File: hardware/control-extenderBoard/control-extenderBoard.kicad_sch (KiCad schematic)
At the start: 117 parts, among them J1 12V + GND (TP), J10 SCL6 + GND (TP), J11 SDA6 + GND (TP), J12 3V3 + GND (TP), J13 12V + GND (TP), J14 SCL6 + GND (TP), J15 SDA6 + GND (TP), J17 24V IN, J18 GND, J2 12V Out, J22 SDA, SCL - ESP32, J23 I2C Reserve SCL/GND, J24 I2C Reserve SCL/GND, J25 I2C Reserve SDA/GND, J26 I2C Reserve SDA/GND, J3 5V out, J4 3V3 + GND (TP), J5 GND, J6 SCL7 Differential (TP), J7 SDA7 Differential (TP), J8 RS485, J9 3V3 out, P1 ISP, U1 MAX3485, U10 LM2576T-12, U2 PCA9600D, U3 TCA9548A_1-to-8_I2C_Multiplex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, U4 LM2576T-3.3, U5 PCA9600D, U6 PCA82C251, U7 PCA82C251, U8 PCA9600D, U9 LM2576T-5

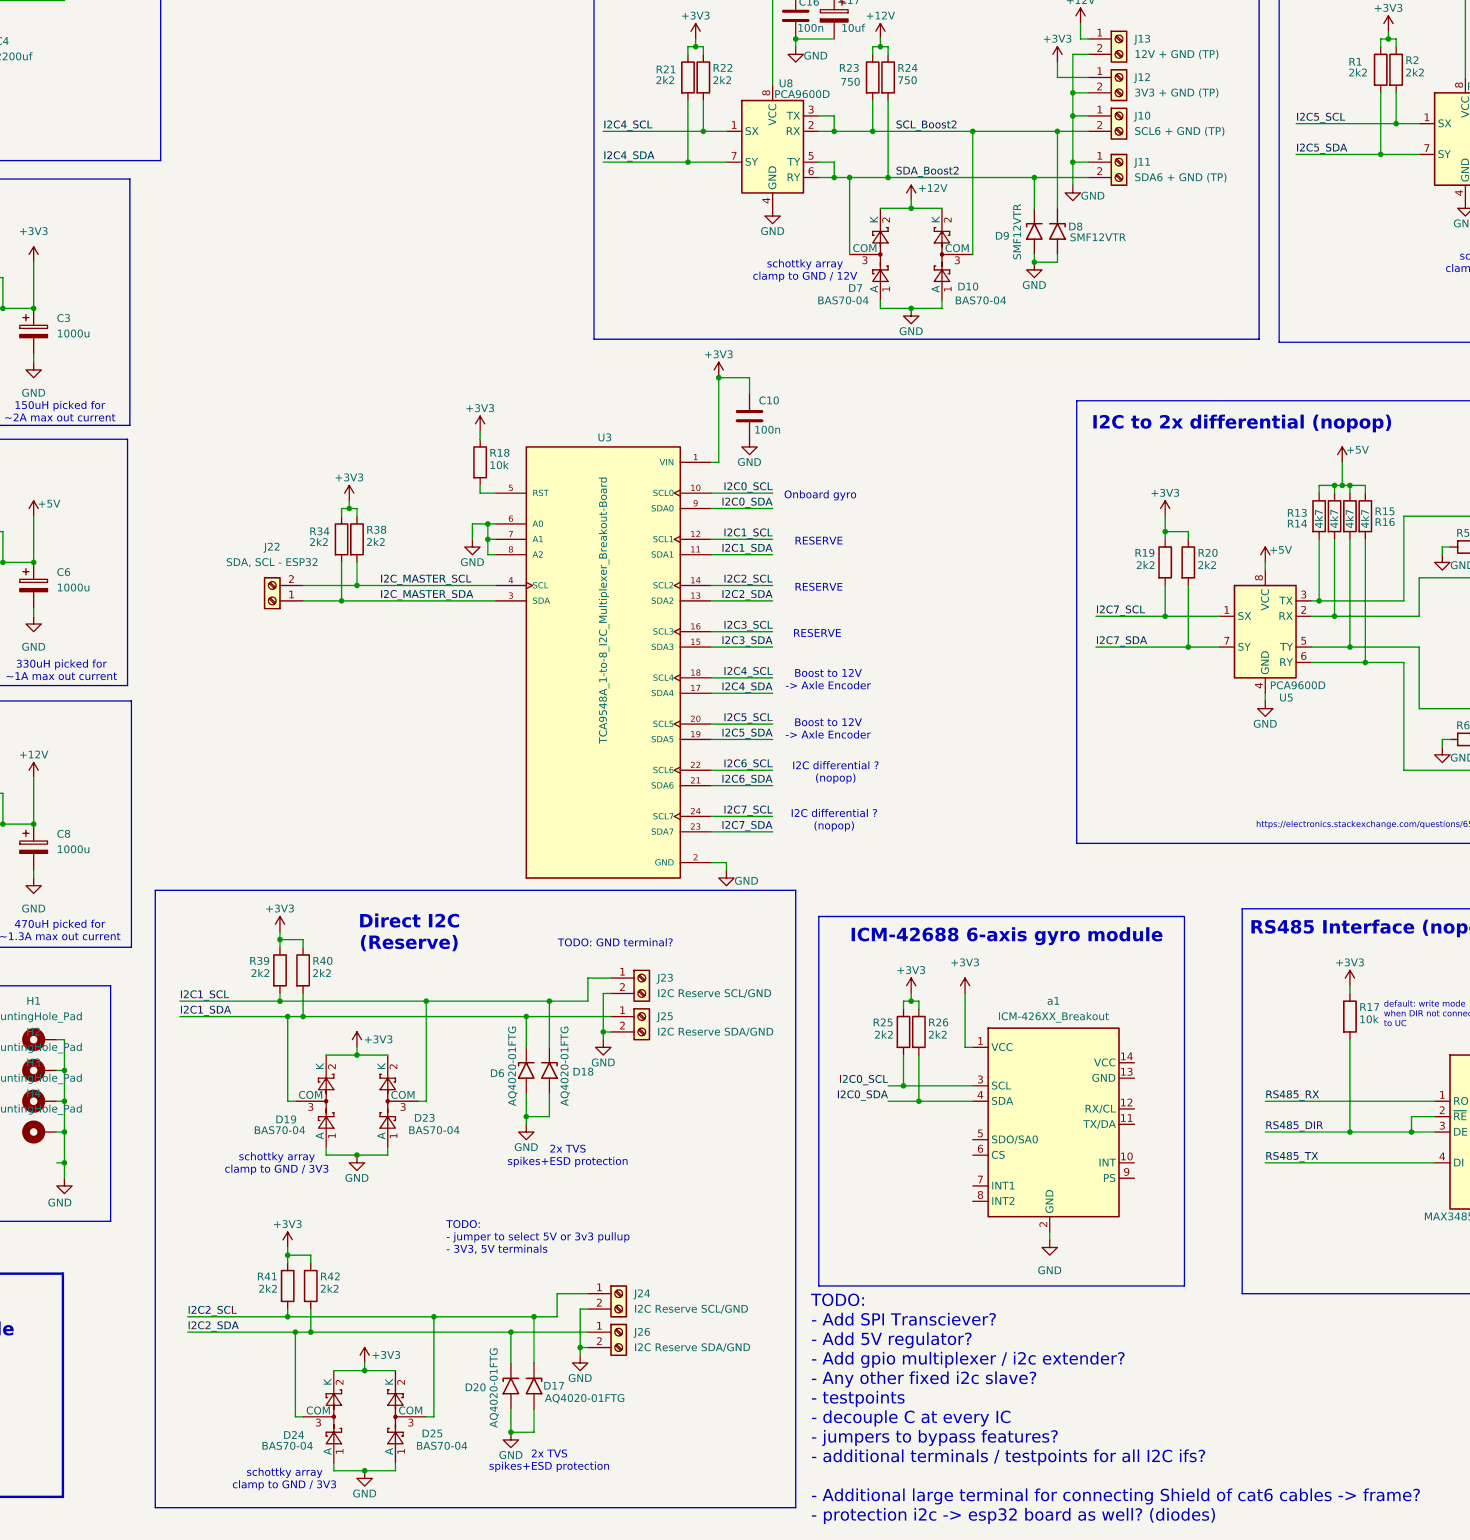
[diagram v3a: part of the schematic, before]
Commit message: extenderBoard: I2C add series Resistors, Add CAT6 Shield, Chassis GND, Arrange vertical R footprints
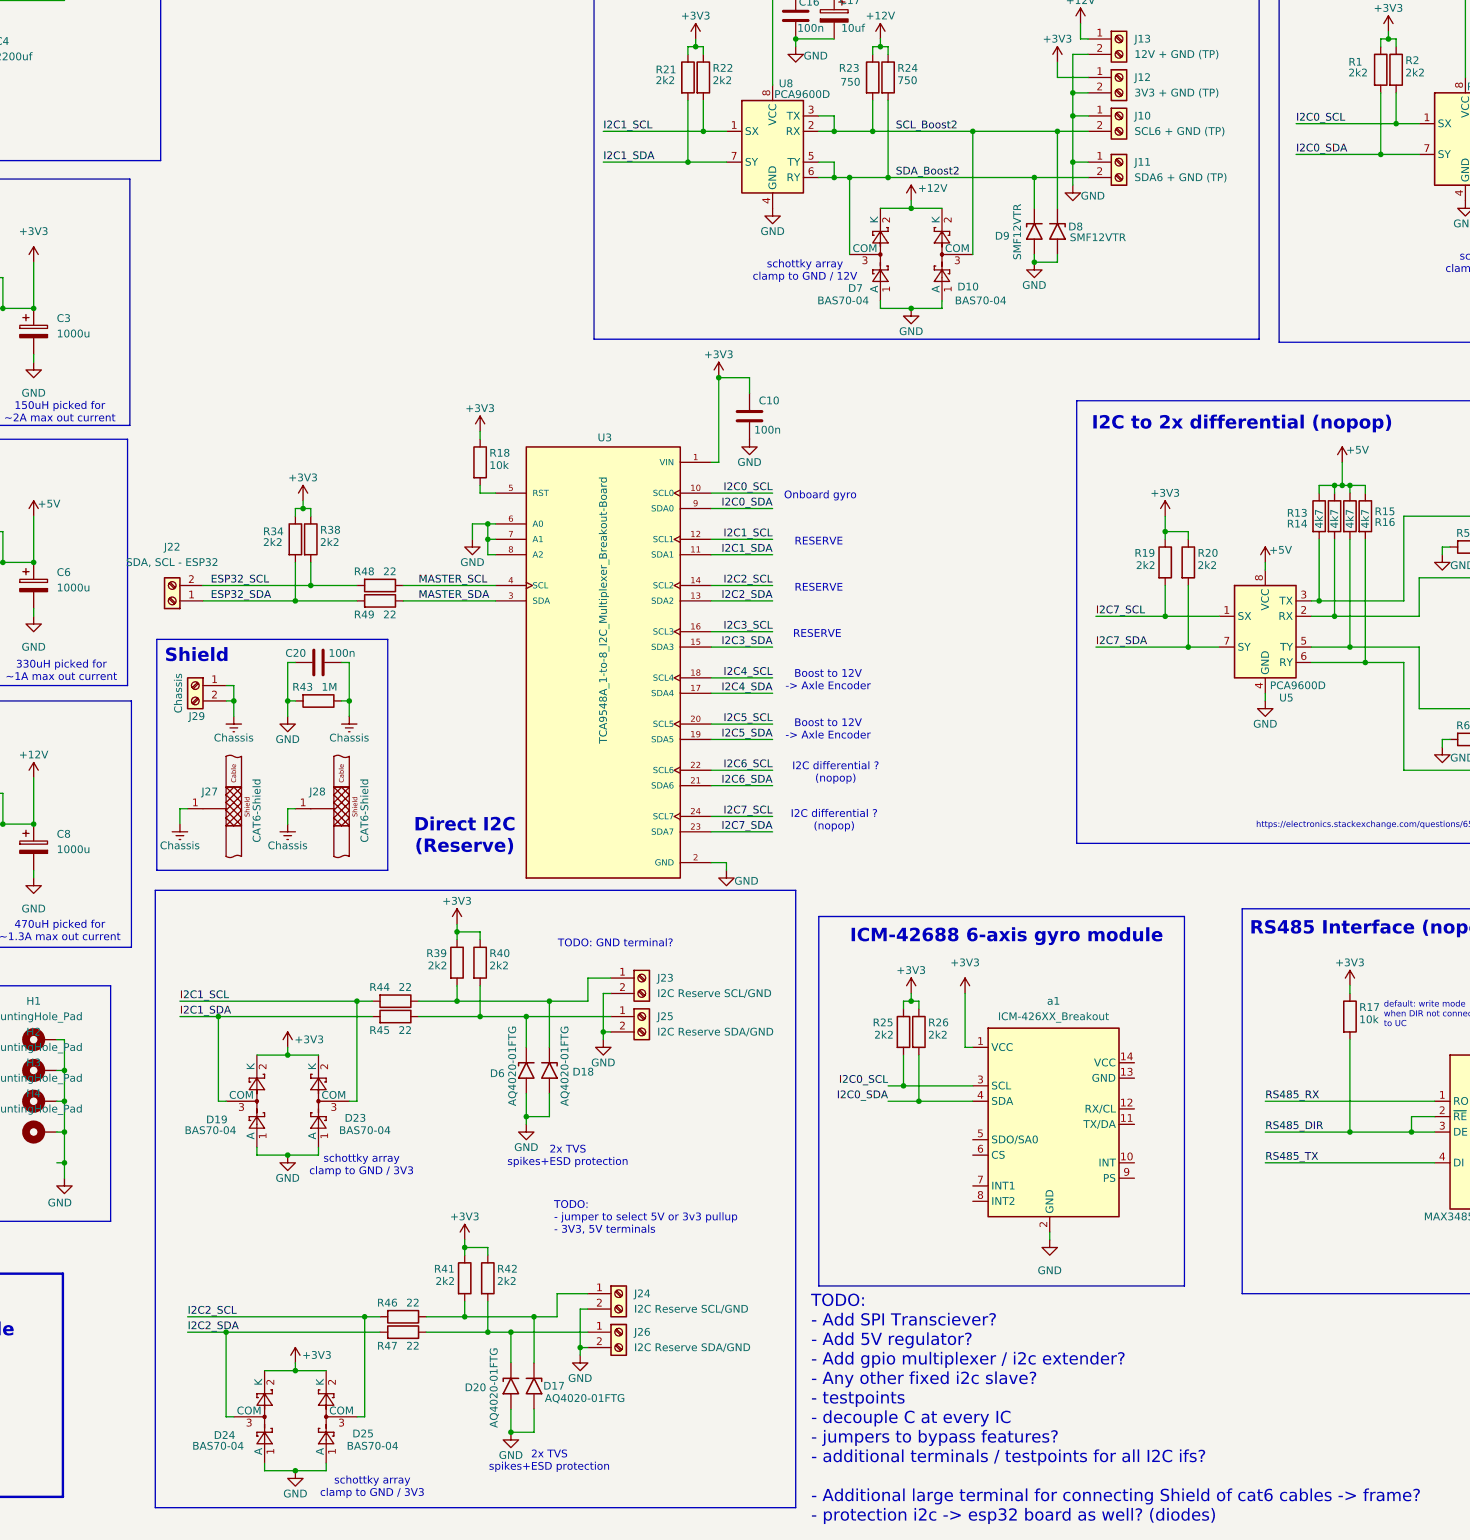
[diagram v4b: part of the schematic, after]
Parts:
- added C20: 100n, Capacitor_THT:C_Disc_D7.0mm_W2.5mm_P5.00mm, symbol Device:C
- added J27, J28: CAT6-Shield, misc_libJonny:Shield_Landing_Pad_6mmCable_ZipTie, symbol misc_libJonny:Shield_Landing_Pad
- added J29: Chassis, terminals_libJonny:ScrewTerminal_P5mm_2Pin_FP10x8, symbol Connector:Screw_Terminal_01x02
- added R43: 1M, Resistor_THT:R_Axial_DIN0207_L6.3mm_D2.5mm_P10.16mm_Horizontal, symbol Device:R
- added R44, R45, R46, R47, R48, R49: 22, Resistor_THT:R_Axial_DIN0207_L6.3mm_D2.5mm_P10.16mm_Horizontal, symbol Device:R
- R34, R38, R39, R40, R41, R42: footprint Resistor_THT:R_Axial_DIN0207_L6.3mm_D2.5mm_P10.16mm_Horizontal -> Resistor_THT:R_Axial_DIN0207_L6.3mm_D2.5mm_P2.54mm_Vertical
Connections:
- net GND: now also C20.1, R43.2
- net I2C0_SCL: now also R2.2, U2.1 (SX)
- net I2C0_SDA: now also R1.2, U2.7 (SY)
- net I2C1_SCL: now also R22.2, U8.1 (SX), R44.2; no longer D18.1 (A1), J23.1 (Pin_1), R39.2
- net I2C1_SDA: now also R21.2, U8.7 (SY), R45.2; no longer D6.1 (A1), J25.1 (Pin_1), R40.2
- net I2C2_SCL: now also R46.2; no longer D17.1 (A1), J24.1 (Pin_1), R41.2
- net I2C2_SDA: now also R47.2; no longer D20.1 (A1), J26.1 (Pin_1), R42.2
- net I2C4_SCL: no longer R22.2, U8.1 (SX)
- net I2C4_SDA: no longer R21.2, U8.7 (SY)
- net I2C5_SCL: no longer R2.2, U2.1 (SX)
- net I2C5_SDA: no longer R1.2, U2.7 (SY)
- net I2C_MASTER_SCL: no longer J22.2 (Pin_2), R38.2, U3.4 (SCL)
- net I2C_MASTER_SDA: no longer J22.1 (Pin_1), R34.2, U3.3 (SDA)
- new net: D18.1 (A1), J23.1 (Pin_1), R39.2, R44.1
- new net: D6.1 (A1), J25.1 (Pin_1), R40.2, R45.1
- new net: D17.1 (A1), J24.1 (Pin_1), R41.2, R46.1
- new net: D20.1 (A1), J26.1 (Pin_1), R42.2, R47.1
- new net Chassis: C20.2, J27.1, J28.1, J29.1 (Pin_1), J29.2 (Pin_2), R43.1
- new net ESP32_SCL: J22.2 (Pin_2), R38.2, R48.2
- new net ESP32_SDA: J22.1 (Pin_1), R34.2, R49.2
- new net MASTER_SCL: R48.1, U3.4 (SCL)
- new net MASTER_SDA: R49.1, U3.3 (SDA)
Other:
- note added: "Shield"
- moved on the sheet: D19, D23, D24, D25, J22, R34, R38, R39, R40, R41, R42

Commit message: extenderBoard: Route supply + regulators
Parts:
- removed J3: 5V out, terminals_libJonny:ScrewTerminal_P5mm_2Pin_FP10x8, symbol Connector:Screw_Terminal_01x02
- removed J9: 3V3 out, terminals_libJonny:ScrewTerminal_P5mm_2Pin_FP10x8, symbol Connector:Screw_Terminal_01x02
- added J30: RX TX, terminals_libJonny:ScrewTerminal_P3.5mm_2Pin_FP7x7, symbol Connector:Screw_Terminal_01x02
- added J31: DIR, GND, terminals_libJonny:ScrewTerminal_P3.5mm_2Pin_FP7x7, symbol Connector:Screw_Terminal_01x02
- added J32: 12V out, terminals_libJonny:ScrewTerminal_P5mm_3Pin_FP15x8, symbol Connector:Screw_Terminal_01x03
- added J33: 5V out, terminals_libJonny:ScrewTerminal_P5mm_3Pin_FP15x8, symbol Connector:Screw_Terminal_01x03
- added J34: 3V3 out, terminals_libJonny:ScrewTerminal_P5mm_3Pin_FP15x8, symbol Connector:Screw_Terminal_01x03
- D2, D5: footprint Diode_THT:D_DO-201AD_P15.24mm_Horizontal -> Diode_THT:D_DO-201AE_P5.08mm_Vertical_AnodeUp
- J2: value 12V Out -> GND
- R39, R40, R41, R42: footprint Resistor_THT:R_Axial_DIN0207_L6.3mm_D2.5mm_P2.54mm_Vertical -> Resistor_THT:R_Axial_DIN0207_L6.3mm_D2.5mm_P10.16mm_Horizontal
- U1: footprint modules_libJonny:Adapter-Board_SOP8_to_DIP8 -> Package_DIP:DIP-8_W7.62mm_LongPads
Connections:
- net +12V: now also J32.1 (Pin_1), J32.2 (Pin_2), J32.3 (Pin_3); no longer J2.1 (Pin_1), J2.2 (Pin_2)
- net +3V3: now also J34.1 (Pin_1), J34.2 (Pin_2), J34.3 (Pin_3)
- net +5V: now also J33.1 (Pin_1), J33.2 (Pin_2), J33.3 (Pin_3)
- net GND: now also J2.1 (Pin_1), J2.2 (Pin_2), J31.1 (Pin_1)
- net I2C0_SCL: no longer R25.2, a1.3 (SCL)
- net I2C0_SDA: no longer R26.2, a1.4 (SDA)
- net I2C1_SCL: no longer D23.3 (COM), R44.2
- net I2C1_SDA: no longer D19.3 (COM), R45.2
- net I2C2_SCL: no longer D25.3 (COM), R46.2
- net I2C2_SDA: no longer D24.3 (COM), R47.2
- net I2C5_SCL: now also R25.2, a1.3 (SCL)
- net I2C5_SDA: now also R26.2, a1.4 (SDA)
- net I2C6_SCL: now also D25.3 (COM), R46.2
- net I2C6_SDA: now also D24.3 (COM), R47.2
- net I2C7_SCL: now also D23.3 (COM), R44.2
- net I2C7_SDA: now also D19.3 (COM), R45.2
- net RS485_DIR: now also J30.1 (Pin_1)
- net RS485_RX: now also J30.2 (Pin_2)
- net RS485_TX: now also J31.2 (Pin_2)
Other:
- moved on the sheet: J5

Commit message: extenderBoard: Route I2C 12V boosting
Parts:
- R48, R49: footprint Resistor_THT:R_Axial_DIN0207_L6.3mm_D2.5mm_P10.16mm_Horizontal -> Resistor_THT:R_Axial_DIN0204_L3.6mm_D1.6mm_P7.62mm_Horizontal
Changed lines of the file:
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@@
 			)
 		)
-		(property "Footprint" "Resistor_THT:R_Axial_DIN0207_L6.3mm_D2.5mm_P10.16mm_Horizontal"
+		(property "Footprint" "Resistor_THT:R_Axial_DIN0204_L3.6mm_D1.6mm_P7.62mm_Horizontal"
 			(at 146.05 135.128 90)
 			(effects
@@
 			)
 		)
-		(property "Footprint" "Resistor_THT:R_Axial_DIN0207_L6.3mm_D2.5mm_P10.16mm_Horizontal"
+		(property "Footprint" "Resistor_THT:R_Axial_DIN0204_L3.6mm_D1.6mm_P7.62mm_Horizontal"
 			(at 146.05 129.032 90)
 			(effects

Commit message: extenderBoard: Route RS485, I2C reserve, Add Testpoints, GND-Zones
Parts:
- removed J2: GND, terminals_libJonny:ScrewTerminal_P5mm_2Pin_FP10x8, symbol Connector:Screw_Terminal_01x02
- removed P1: ISP, Connector_IDC:IDC-Header_2x05_P2.54mm_Vertical, symbol control-rescue:CONN_5X2
- added J3, J35, J36, J37, J38, J39: Conn_01x02_Pin, Connector_PinHeader_2.54mm:PinHeader_1x02_P2.54mm_Vertical, symbol Connector:Conn_01x02_Pin
- added J9: Conn_01x03_Pin, Connector_PinHeader_2.54mm:PinHeader_1x03_P2.54mm_Vertical, symbol Connector:Conn_01x03_Pin
- added TP10: 12V, Connector_PinHeader_2.54mm:PinHeader_1x01_P2.54mm_Vertical, symbol Connector:TestPoint
- added TP11: 3V3, Connector_PinHeader_2.54mm:PinHeader_1x01_P2.54mm_Vertical, symbol Connector:TestPoint
- added TP13, TP8: GND, Connector_PinHeader_2.54mm:PinHeader_1x01_P2.54mm_Vertical, symbol Connector:TestPoint
- added TP14, TP16: SCL6, Connector_PinHeader_2.54mm:PinHeader_1x01_P2.54mm_Vertical, symbol Connector:TestPoint
- added TP15, TP17: SDA6, Connector_PinHeader_2.54mm:PinHeader_1x01_P2.54mm_Vertical, symbol Connector:TestPoint
- added TP18: Chassis, Connector_PinHeader_2.54mm:PinHeader_1x01_P2.54mm_Vertical, symbol Connector:TestPoint
- added TP2: RX, Connector_PinHeader_2.54mm:PinHeader_1x01_P2.54mm_Vertical, symbol Connector:TestPoint
- added TP4: DE, Connector_PinHeader_2.54mm:PinHeader_1x01_P2.54mm_Vertical, symbol Connector:TestPoint
- added TP7: TX, Connector_PinHeader_2.54mm:PinHeader_1x01_P2.54mm_Vertical, symbol Connector:TestPoint
- added TP9: 5V, Connector_PinHeader_2.54mm:PinHeader_1x01_P2.54mm_Vertical, symbol Connector:TestPoint
- J24: value I2C Reserve SCL/GND -> I2C Reserve SDA/GND
- J26: value I2C Reserve SDA/GND -> I2C Reserve SCL/GND
- R36: footprint Resistor_THT:R_Axial_DIN0207_L6.3mm_D2.5mm_P2.54mm_Vertical -> Resistor_THT:R_Axial_DIN0207_L6.3mm_D2.5mm_P10.16mm_Horizontal
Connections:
- net +12V: now also TP10.1
- net +3V3: now also TP11.1
- net +5V: now also TP9.1
- net Chassis: now also TP18.1
- net GND: now also TP13.1, TP8.1
- net I2C0_SCL: now also J39.1 (Pin_1)
- net I2C0_SDA: now also J39.2 (Pin_2)
- net I2C1_SCL: now also J38.1 (Pin_1)
- net I2C1_SDA: now also J38.2 (Pin_2)
- net I2C2_SCL: now also J3.1 (Pin_1)
- net I2C2_SDA: now also J3.2 (Pin_2)
- net I2C3_SCL: now also J35.1 (Pin_1)
- net I2C3_SDA: now also J35.2 (Pin_2)
- net I2C4_SCL: now also J36.1 (Pin_1)
- net I2C4_SDA: now also J36.2 (Pin_2)
- net I2C5_SCL: now also J37.1 (Pin_1)
- net I2C5_SDA: now also J37.2 (Pin_2)
- net RS485_DIR: now also TP4.1
- net RS485_RX: now also TP2.1
- net RS485_TX: now also TP7.1
- net at D18.1 (A1), J23.1 (Pin_1), R39.2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: now also TP16.1
- net at D6.1 (A1), J25.1 (Pin_1), R40.2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: now also TP17.1
- net at R41.2, R46.1: now also D20.1 (A1), J26.1 (Pin_1), TP14.1; no longer D17.1 (A1), J24.1 (Pin_1)
- net at R42.2, R47.1: now also D17.1 (A1), J24.1 (Pin_1), TP15.1; no longer D20.1 (A1), J26.1 (Pin_1)
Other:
- note added: "RESERVE (pullup, protection, screw-terminal)"
- note added: "RS485 Interface"
- note added: "UNUSED / RESERVE"
- note removed: "Interface to control board (ESP32)"
- note removed: "RESERVE"
- note removed: "RS485 Interface (nopop)"
- moved on the sheet: D17, D20, J18, J24, J26, J32, J33, J34, J5
